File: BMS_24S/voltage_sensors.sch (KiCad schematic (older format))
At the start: 27 parts, among them J401 VOLT_IDC_26_CONN

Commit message: update balancing circuit
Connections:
- net CELL_13: no longer F408.2, F410.2
- net CELL_21: now reaches F402.2
- net CELL_22: now reaches F404.2
- net CELL_23: now reaches F406.2
- new net CELL_24: F408.2
- no-connect marks 3 -> 1
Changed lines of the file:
@@
 $Descr User 8268 5827
 encoding utf-8
-Sheet 4 32
+Sheet 4 31
 Title ""
 Date ""
@@
 Text Label 2100 800  0    50   ~ 0
 1.8V
-Text HLabel 2100 900  2    50   Input ~ 0
+Text HLabel 2100 900  2    50   Output ~ 0
 V1
-Text HLabel 2100 1000 2    50   Input ~ 0
+Text HLabel 2100 1000 2    50   Output ~ 0
 V2
 Text Label 900  800  2    50   ~ 0
@@
 Text Label 2100 1500 0    50   ~ 0
 1.8V
-Text HLabel 2100 1600 2    50   Input ~ 0
+Text HLabel 2100 1600 2    50   Output ~ 0
 V3
-Text HLabel 2100 1700 2    50   Input ~ 0
+Text HLabel 2100 1700 2    50   Output ~ 0
 V4
 Text Label 900  1500 2    50   ~ 0
@@
 Text Label 2100 2200 0    50   ~ 0
 1.8V
-Text HLabel 2100 2300 2    50   Input ~ 0
+Text HLabel 2100 2300 2    50   Output ~ 0
 V5
-Text HLabel 2100 2400 2    50   Input ~ 0
+Text HLabel 2100 2400 2    50   Output ~ 0
 V6
 Text Label 900  2200 2    50   ~ 0
@@
 Text Label 2100 2900 0    50   ~ 0
 1.8V
-Text HLabel 2100 3000 2    50   Input ~ 0
+Text HLabel 2100 3000 2    50   Output ~ 0
 V7
-Text HLabel 2100 3100 2    50   Input ~ 0
+Text HLabel 2100 3100 2    50   Output ~ 0
 V8
 Text Label 900  2900 2    50   ~ 0
@@
 Text Label 2100 3600 0    50   ~ 0
 1.8V
-Text HLabel 2100 3700 2    50   Input ~ 0
+Text HLabel 2100 3700 2    50   Output ~ 0
 V9
-Text HLabel 2100 3800 2    50   Input ~ 0
+Text HLabel 2100 3800 2    50   Output ~ 0
 V10
 Text Label 900  3600 2    50   ~ 0
@@
 CELL_10
 $Sheet
-S 1000 4150 1000 500
+S 2850 650  1000 500
 U 5ED048B6
 F0 "voltage_11_12" 50
-F1 "voltage_1_2.sch" 50
-F2 "cell_01" I L 1000 4400 50
-F3 "cell_02" I L 1000 4500 50
-F4 "1.8V" I R 2000 4300 50
-F5 "cell_gnd" I L 1000 4300 50
-F6 "V_02" O R 2000 4500 50
-F7 "V_01" O R 2000 4400 50
-$EndSheet
-Wire Wire Line
-	2000 4300 2100 4300
-Wire Wire Line
-	2000 4400 2100 4400
-Wire Wire Line
-	2000 4500 2100 4500
-Wire Wire Line
-	1000 4300 900  4300
-Wire Wire Line
-	1000 4400 900  4400
-Wire Wire Line
-	1000 4500 900  4500
-Text Label 2100 4300 0    50   ~ 0
-1.8V
-Text HLabel 2100 4400 2    50   Input ~ 0
-V11
-Text HLabel 2100 4500 2    50   Input ~ 0
-V12
-Text Label 900  4300 2    50   ~ 0
-CELL_10
-Text Label 900  4400 2    50   ~ 0
-CELL_11
-Text Label 900  4500 2    50   ~ 0
-CELL_12
-$Sheet
-S 2850 650  1000 500
-U 5ED0B726
-F0 "voltage_13_14" 50
 F1 "voltage_1_2.sch" 50
 F2 "cell_01" I L 2850 900 50
@@
 Text Label 3950 800  0    50   ~ 0
 1.8V
-Text HLabel 3950 900  2    50   Input ~ 0
-V13
-Text HLabel 3950 1000 2    50   Input ~ 0
-V14
+Text HLabel 3950 900  2    50   Output ~ 0
+V11
+Text HLabel 3950 1000 2    50   Output ~ 0
+V12
 Text Label 2750 800  2    50   ~ 0
+CELL_10
+Text Label 2750 900  2    50   ~ 0
+CELL_11
+Text Label 2750 1000 2    50   ~ 0
 CELL_12
-Text Label 2750 900  2    50   ~ 0
-CELL_13
-Text Label 2750 1000 2    50   ~ 0
-CELL_14
 $Sheet
 S 2850 1350 1000 500
-U 5ED0B73A
-F0 "voltage_15_16" 50
+U 5ED0B726
+F0 "voltage_13_14" 50
 F1 "voltage_1_2.sch" 50
 F2 "cell_01" I L 2850 1600 50
@@
 Text Label 3950 1500 0    50   ~ 0
 1.8V
-Text HLabel 3950 1600 2    50   Input ~ 0
-V15
-Text HLabel 3950 1700 2    50   Input ~ 0
-V16
+Text HLabel 3950 1600 2    50   Output ~ 0
+V13
+Text HLabel 3950 1700 2    50   Output ~ 0
+V14
 Text Label 2750 1500 2    50   ~ 0
+CELL_12
+Text Label 2750 1600 2    50   ~ 0
+CELL_13
+Text Label 2750 1700 2    50   ~ 0
 CELL_14
-Text Label 2750 1600 2    50   ~ 0
-CELL_15
-Text Label 2750 1700 2    50   ~ 0
-CELL_16
 $Sheet
 S 2850 2050 1000 500
-U 5ED0B74E
-F0 "voltage_17_18" 50
+U 5ED0B73A
+F0 "voltage_15_16" 50
 F1 "voltage_1_2.sch" 50
 F2 "cell_01" I L 2850 2300 50
@@
 Text Label 3950 2200 0    50   ~ 0
 1.8V
-Text HLabel 3950 2300 2    50   Input ~ 0
-V17
-Text HLabel 3950 2400 2    50   Input ~ 0
-V18
+Text HLabel 3950 2300 2    50   Output ~ 0
+V15
+Text HLabel 3950 2400 2    50   Output ~ 0
+V16
 Text Label 2750 2200 2    50   ~ 0
+CELL_14
+Text Label 2750 2300 2    50   ~ 0
+CELL_15
+Text Label 2750 2400 2    50   ~ 0
 CELL_16
-Text Label 2750 2300 2    50   ~ 0
-CELL_17
-Text Label 2750 2400 2    50   ~ 0
-CELL_18
 $Sheet
 S 2850 2750 1000 500
-U 5ED0B762
-F0 "voltage_19_20" 50
+U 5ED0B74E
+F0 "voltage_17_18" 50
 F1 "voltage_1_2.sch" 50
 F2 "cell_01" I L 2850 3000 50
@@
 Text Label 3950 2900 0    50   ~ 0
 1.8V
-Text HLabel 3950 3000 2    50   Input ~ 0
+Text HLabel 3950 3000 2    50   Output ~ 0
+V17
+Text HLabel 3950 3100 2    50   Output ~ 0
+V18
+Text Label 2750 2900 2    50   ~ 0
+CELL_16
+Text Label 2750 3000 2    50   ~ 0
+CELL_17
+Text Label 2750 3100 2    50   ~ 0
+CELL_18
+$Sheet
+S 2850 3450 1000 500
+U 5ED0B762
+F0 "voltage_19_20" 50
+F1 "voltage_1_2.sch" 50
+F2 "cell_01" I L 2850 3700 50
+F3 "cell_02" I L 2850 3800 50
+F4 "1.8V" I R 3850 3600 50
+F5 "cell_gnd" I L 2850 3600 50
+F6 "V_02" O R 3850 3800 50
+F7 "V_01" O R 3850 3700 50
+$EndSheet
+Wire Wire Line
+	3850 3600 3950 3600
+Wire Wire Line
+	3850 3700 3950 3700
+Wire Wire Line
+	3850 3800 3950 3800
+Wire Wire Line
+	2850 3600 2750 3600
+Wire Wire Line
+	2850 3700 2750 3700
+Wire Wire Line
+	2850 3800 2750 3800
+Text Label 3950 3600 0    50   ~ 0
+1.8V
+Text HLabel 3950 3700 2    50   Output ~ 0
 V19
-Text HLabel 3950 3100 2    50   Input ~ 0
+Text HLabel 3950 3800 2    50   Output ~ 0
 V20
-Text Label 2750 2900 2    50   ~ 0
+Text Label 2750 3600 2    50   ~ 0
 CELL_18
-Text Label 2750 3000 2    50   ~ 0
+Text Label 2750 3700 2    50   ~ 0
 CELL_19
-Text Label 2750 3100 2    50   ~ 0
+Text Label 2750 3800 2    50   ~ 0
 CELL_20
 $Comp
@@
 Text GLabel 6700 2700 0    50   Input ~ 0
 CELL_12
-Text GLabel 6700 2000 0    50   Input ~ 0
-CELL_13
-Text GLabel 6700 1800 0    50   Input ~ 0
-CELL_13
 $Comp
 L Connector:Conn_01x26_Female J?
@@
 Text GLabel 6700 1100 0    50   Input ~ 0
 CELL_20
-NoConn ~ 6700 1600
-NoConn ~ 6700 1400
-NoConn ~ 6700 1200
+$Sheet
+S 4750 650  1000 500
+U 5F489B81
+F0 "voltage_21_22" 50
+F1 "voltage_1_2.sch" 50
+F2 "cell_01" I L 4750 900 50
+F3 "cell_02" I L 4750 1000 50
+F4 "1.8V" I R 5750 800 50
+F5 "cell_gnd" I L 4750 800 50
+F6 "V_02" O R 5750 1000 50
+F7 "V_01" O R 5750 900 50
+$EndSheet
+Wire Wire Line
+	5750 800  5850 800
+Wire Wire Line
+	5750 900  5850 900
+Wire Wire Line
+	5750 1000 5850 1000
+Wire Wire Line
+	4750 800  4650 800
+Wire Wire Line
+	4750 900  4650 900
+Wire Wire Line
+	4750 1000 4650 1000
+Text Label 5850 800  0    50   ~ 0
+1.8V
+Text HLabel 5850 900  2    50   Output ~ 0
+V21
+Text HLabel 5850 1000 2    50   Output ~ 0
+V22
+Text Label 4650 800  2    50   ~ 0
+CELL_20
+Text Label 4650 900  2    50   ~ 0
+CELL_21
+Text Label 4650 1000 2    50   ~ 0
+CELL_22
+$Sheet
+S 4750 1350 1000 500
+U 5F489B95
+F0 "voltage_23_24" 50
+F1 "voltage_1_2.sch" 50
+F2 "cell_01" I L 4750 1600 50
+F3 "cell_02" I L 4750 1700 50
+F4 "1.8V" I R 5750 1500 50
+F5 "cell_gnd" I L 4750 1500 50
+F6 "V_02" O R 5750 1700 50
+F7 "V_01" O R 5750 1600 50
+$EndSheet
+Wire Wire Line
+	5750 1500 5850 1500
+Wire Wire Line
+	5750 1600 5850 1600
+Wire Wire Line
+	5750 1700 5850 1700
+Wire Wire Line
+	4750 1500 4650 1500
+Wire Wire Line
+	4750 1600 4650 1600
+Wire Wire Line
+	4750 1700 4650 1700
+Text Label 5850 1500 0    50   ~ 0
+1.8V
+Text HLabel 5850 1600 2    50   Output ~ 0
+V23
+Text HLabel 5850 1700 2    50   Output ~ 0
+V24
+Text Label 4650 1500 2    50   ~ 0
+CELL_22
+Text Label 4650 1600 2    50   ~ 0
+CELL_23
+Text Label 4650 1700 2    50   ~ 0
+CELL_24
+Text GLabel 6700 1200 0    50   Input ~ 0
+CELL_21
+Text GLabel 6700 1400 0    50   Input ~ 0
+CELL_22
+Text GLabel 6700 1600 0    50   Input ~ 0
+CELL_23
+Text GLabel 6700 1800 0    50   Input ~ 0
+CELL_24
+NoConn ~ 6700 2000
 $EndSCHEMATC

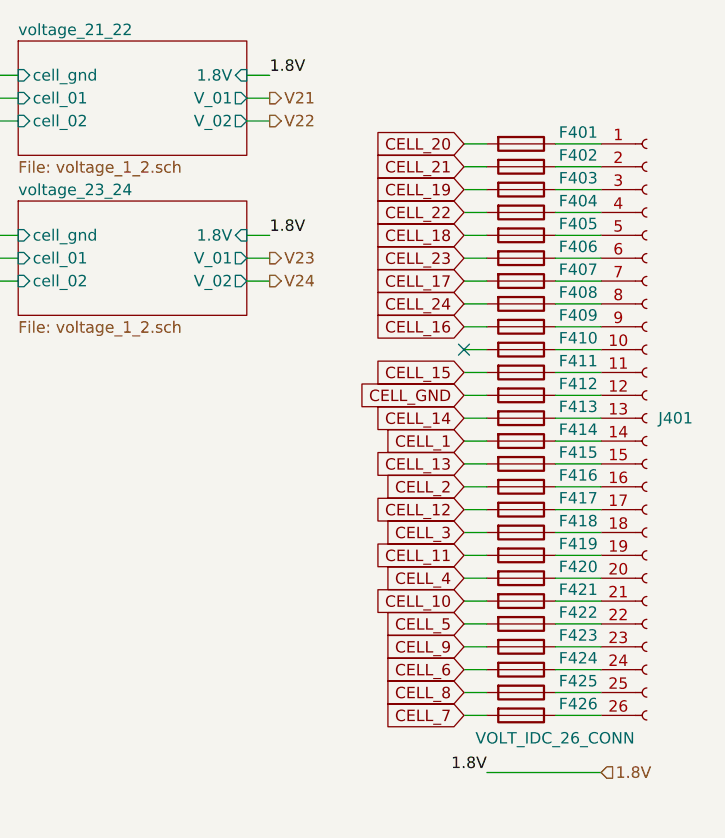
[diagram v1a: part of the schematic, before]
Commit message: updates made on BMS
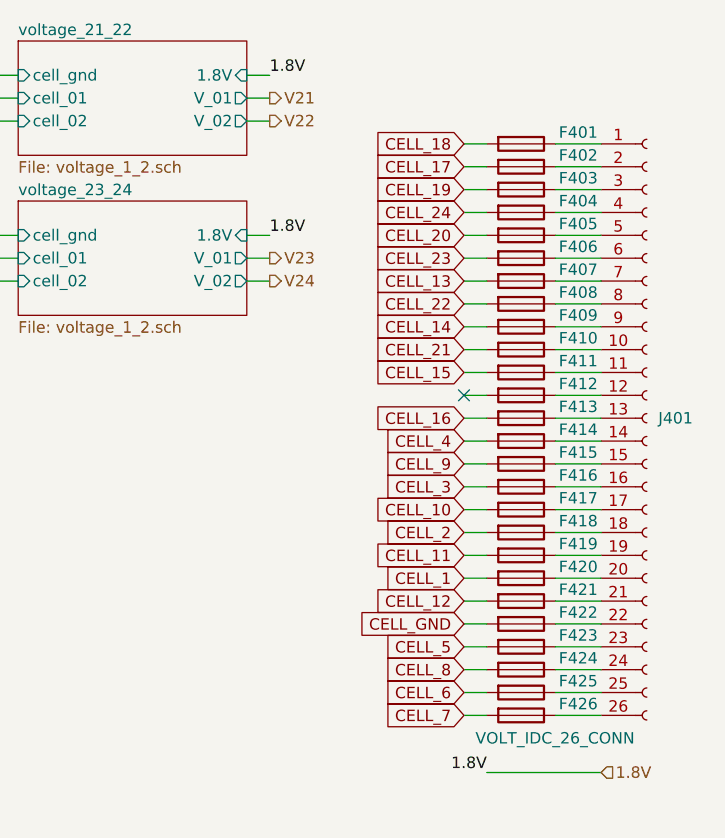
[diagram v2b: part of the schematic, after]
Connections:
- net CELL_1: now also F420.2; no longer F414.2
- net CELL_10: now also F417.2; no longer F421.2
- net CELL_12: now also F421.2; no longer F417.2
- net CELL_13: now also F407.2; no longer F415.2
- net CELL_14: now also F409.2; no longer F413.2
- net CELL_16: now also F413.2; no longer F409.2
- net CELL_17: now also F402.2; no longer F407.2
- net CELL_18: now also F401.2; no longer F405.2
- net CELL_2: now also F418.2; no longer F416.2
- net CELL_20: now also F405.2; no longer F401.2
- net CELL_21: now also F410.2; no longer F402.2
- net CELL_22: now also F408.2; no longer F404.2
- net CELL_24: now also F404.2; no longer F408.2
- net CELL_3: now also F416.2; no longer F418.2
- net CELL_4: now also F414.2; no longer F420.2
- net CELL_5: now also F423.2; no longer F422.2
- net CELL_6: now also F425.2; no longer F424.2
- net CELL_8: now also F424.2; no longer F425.2
- net CELL_9: now also F415.2; no longer F423.2
- net CELL_GND: now also F422.2; no longer F412.2
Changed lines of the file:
@@
 Wire Wire Line
 	7100 2000 7300 2000
-Text GLabel 6700 2900 0    50   Input ~ 0
-CELL_11
-Text GLabel 6700 2400 0    50   Input ~ 0
-CELL_1
-Text GLabel 6700 2600 0    50   Input ~ 0
-CELL_2
-Text GLabel 6700 3100 0    50   Input ~ 0
-CELL_10
-Text GLabel 6700 2800 0    50   Input ~ 0
-CELL_3
-Text GLabel 6700 3300 0    50   Input ~ 0
-CELL_9
-Text GLabel 6700 3000 0    50   Input ~ 0
-CELL_4
-Text GLabel 6700 3500 0    50   Input ~ 0
-CELL_8
-Text GLabel 6700 3200 0    50   Input ~ 0
-CELL_5
-Text GLabel 6700 3600 0    50   Input ~ 0
-CELL_7
-Text GLabel 6700 3400 0    50   Input ~ 0
-CELL_6
-Text GLabel 6700 1300 0    50   Input ~ 0
-CELL_19
-Text GLabel 6700 1500 0    50   Input ~ 0
+Text GLabel 6700 1100 0    50   Input ~ 0
 CELL_18
-Text GLabel 6700 1700 0    50   Input ~ 0
+Text GLabel 6700 1200 0    50   Input ~ 0
 CELL_17
-Text GLabel 6700 1900 0    50   Input ~ 0
-CELL_16
-Text GLabel 6700 2100 0    50   Input ~ 0
-CELL_15
-Text GLabel 6700 2300 0    50   Input ~ 0
-CELL_14
-Text GLabel 6700 2200 0    50   Input ~ 0
-CELL_GND
-Text GLabel 6700 2500 0    50   Input ~ 0
-CELL_13
-Text GLabel 6700 2700 0    50   Input ~ 0
-CELL_12
 $Comp
 L Connector:Conn_01x26_Female J?
@@
 	1    0    0    -1
 $EndComp
-Text GLabel 6700 1100 0    50   Input ~ 0
-CELL_20
 $Sheet
 S 4750 650  1000 500
@@
 Text Label 4650 1700 2    50   ~ 0
 CELL_24
-Text GLabel 6700 1200 0    50   Input ~ 0
+Text GLabel 6700 2000 0    50   Input ~ 0
 CELL_21
-Text GLabel 6700 1400 0    50   Input ~ 0
-CELL_22
 Text GLabel 6700 1600 0    50   Input ~ 0
 CELL_23
+Text GLabel 6700 1400 0    50   Input ~ 0
+CELL_24
+NoConn ~ 6700 2200
 Text GLabel 6700 1800 0    50   Input ~ 0
-CELL_24
-NoConn ~ 6700 2000
+CELL_22
+Text GLabel 6700 1300 0    50   Input ~ 0
+CELL_19
+Text GLabel 6700 1500 0    50   Input ~ 0
+CELL_20
+Text GLabel 6700 1700 0    50   Input ~ 0
+CELL_13
+Text GLabel 6700 1900 0    50   Input ~ 0
+CELL_14
+Text GLabel 6700 2100 0    50   Input ~ 0
+CELL_15
+Text GLabel 6700 2300 0    50   Input ~ 0
+CELL_16
+Text GLabel 6700 2500 0    50   Input ~ 0
+CELL_9
+Text GLabel 6700 2700 0    50   Input ~ 0
+CELL_10
+Text GLabel 6700 2900 0    50   Input ~ 0
+CELL_11
+Text GLabel 6700 3100 0    50   Input ~ 0
+CELL_12
+Text GLabel 6700 3300 0    50   Input ~ 0
+CELL_5
+Text GLabel 6700 3500 0    50   Input ~ 0
+CELL_6
+Text GLabel 6700 3600 0    50   Input ~ 0
+CELL_7
+Text GLabel 6700 3400 0    50   Input ~ 0
+CELL_8
+Text GLabel 6700 3000 0    50   Input ~ 0
+CELL_1
+Text GLabel 6700 2800 0    50   Input ~ 0
+CELL_2
+Text GLabel 6700 2600 0    50   Input ~ 0
+CELL_3
+Text GLabel 6700 2400 0    50   Input ~ 0
+CELL_4
+Text GLabel 6700 3200 0    50   Input ~ 0
+CELL_GND
 $EndSCHEMATC
